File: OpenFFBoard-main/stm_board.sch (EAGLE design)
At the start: 53 parts, among them J1 10118193-0001LF, SW1 TL3342F160QG/TR, SW2 TL3342F160QG/TR, U1 STM32(LQFP64), U2 NC7NZ17K8X-3-BUFFER, X1 8MHz

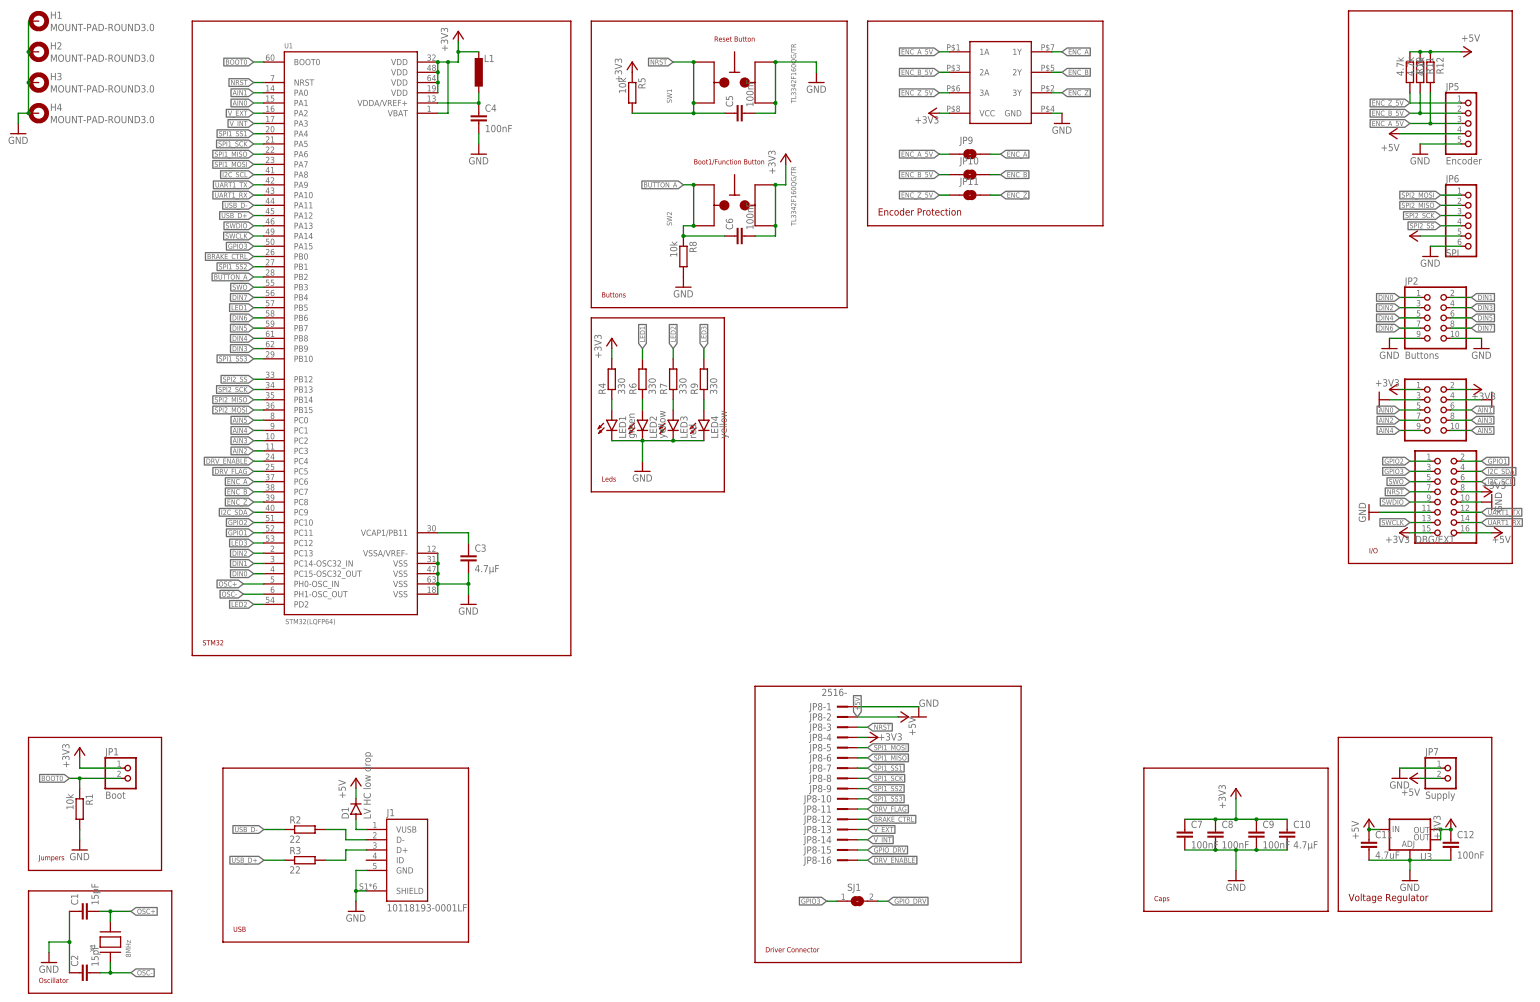
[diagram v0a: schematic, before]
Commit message: Added 1.1.1 stm board
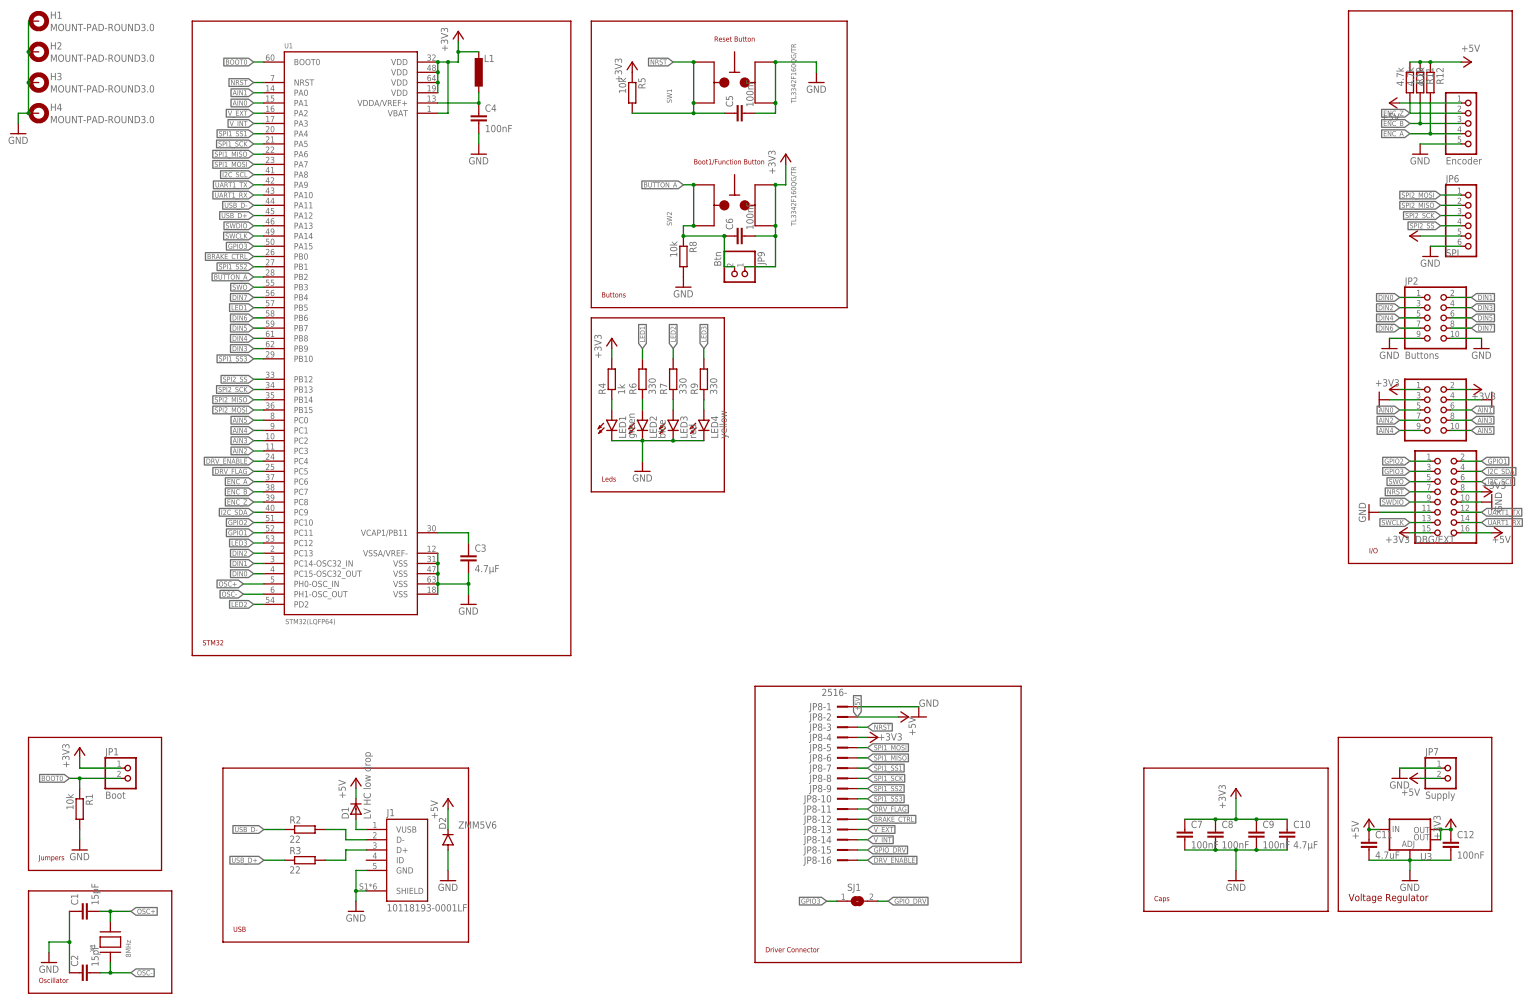
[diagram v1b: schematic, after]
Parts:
- removed JP10, JP11: JUMPER-SMT_2_NO_NO-SILK, SparkFun-Jumpers:JUMPER-SMT_2_NO_NO-SILK
- removed U2: NC7NZ17K8X-3-BUFFER, Powermisc:NC7NZ17K8X-3-BUFFER
- added D2: ZMM5V6, diode:DIODE-MINIMELF
- D1: device diode:DIODE-SOD123 -> adafruit:DIODESMA
- JP9: value JUMPER-SMT_2_NO_NO-SILK -> Btn; device SparkFun-Jumpers:JUMPER-SMT_2_NO_NO-SILK -> pinhead:PINHD-1X2
- LED2: value yellow -> blue
- R4: value 330 -> 1k
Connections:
- removed net ENC_A_5V: JP5.3, JP9.1, R12.2, U2.1A
- removed net ENC_B_5V: JP10.1, JP5.2, R11.2, U2.2A
- removed net ENC_Z_5V: JP11.1, JP5.1, R10.2, U2.3A
- net +3V3: now also JP9.1; no longer U2.VCC
- net +5V: now also D2.C, JP5.1; no longer JP5.4
- net BUTTON_A: now also JP9.2
- net ENC_A: now also JP5.4, R12.2; no longer JP9.2, U2.1Y
- net ENC_B: now also JP5.3, R11.2; no longer JP10.2, U2.2Y
- net ENC_Z: now also JP5.2, R10.2; no longer JP11.2, U2.3Y
- net GND: now also D2.A; no longer U2.GND
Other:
- note removed: "Encoder Protection"
- moved on the sheet: R10, R11, R12
